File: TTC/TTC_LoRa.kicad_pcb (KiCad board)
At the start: 2 copper layers, 70 x 70 mm, 78 parts, among them J1 EPS 3V3, J2 MISSION, J3 SMA edge, J4 SWD TC2030, J5 OBC I2C, J6 OBC UART, J7 EPS 5V, J8 SPARE GPIO, J9 DIPOLE FEED, Q1 AO3401A, U1 TPS7A2033PDBVR, U2 RFM98W-433S2, U3 STM32F446RET6, U4 TMP102, Y1 8MHz, Y2 32.768kHz

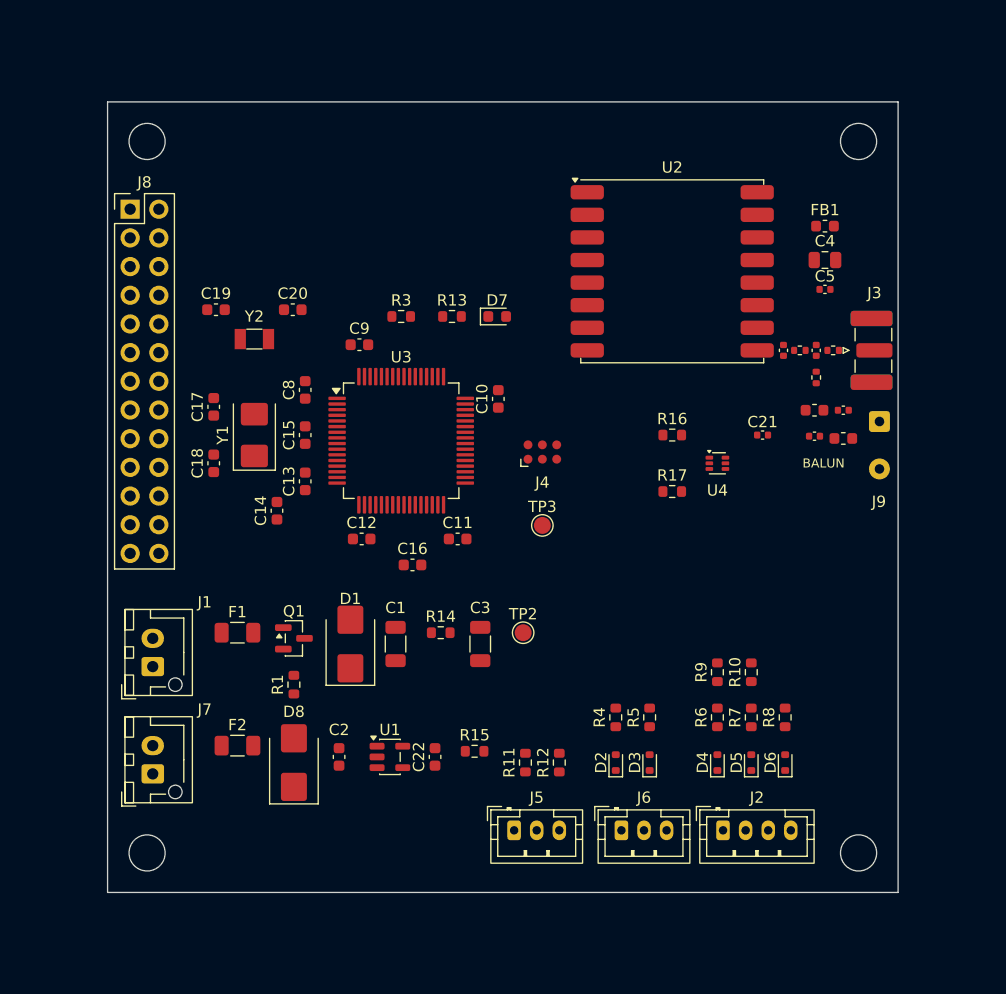
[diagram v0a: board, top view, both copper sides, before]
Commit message: Update ADCS and TTC KiCad designs
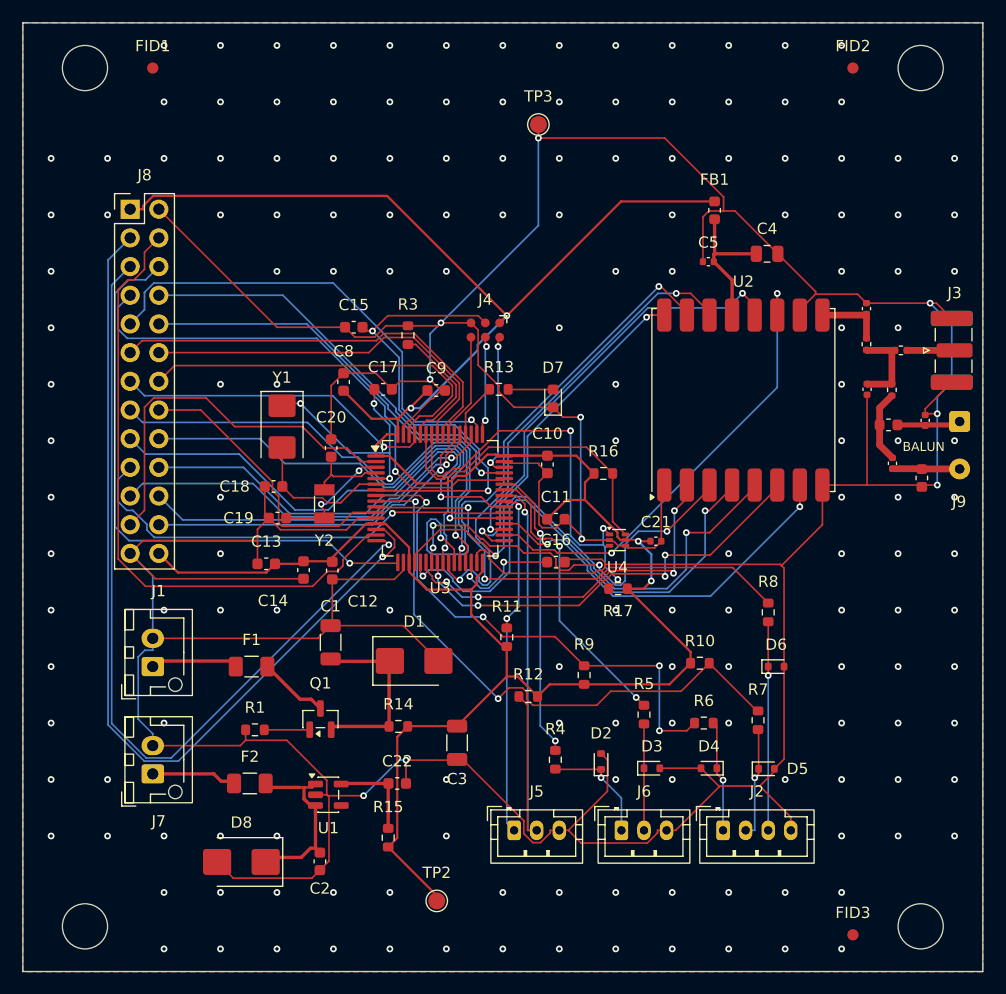
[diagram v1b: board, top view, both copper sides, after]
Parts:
- added FID1: Fiducial, Fiducial_1mm_Mask2mm, F.Cu at (104.0, 97.0)
- added FID2: Fiducial, Fiducial_1mm_Mask2mm, F.Cu at (166.0, 97.0)
- added FID3: Fiducial, Fiducial_1mm_Mask2mm, F.Cu at (166.0, 173.8)
- H1, H2, H3, H4: value M3 -> M4 stack; footprint MountingHole_3.2mm_M3 -> MountingHole_4mm
- moved TP3 35.5 mm to (138.2, 102.0), turned to -90 degrees
- moved TP2 25.0 mm to (129.2, 170.8), turned to 180 degrees
- moved C19 19.2 mm to (115.0, 136.8)
- moved Y2 15.9 mm to (119.2, 135.6), turned to -90 degrees
- moved C17 15.1 mm to (124.4, 125.5), turned to 180 degrees
- moved C21 13.3 mm to (148.6, 138.9)
- moved U2 13.0 mm to (156.3, 126.4), turned to 90 degrees
- moved C20 12.7 mm to (119.8, 130.7), turned to -90 degrees
- moved C16 12.7 mm to (139.7, 140.8)
- moved J4 11.9 mm to (133.4, 120.2), turned to 180 degrees
- moved R9 11.8 mm to (142.2, 150.8)
- moved R11 11.2 mm to (135.3, 147.4)
- moved U4 11.2 mm to (145.2, 138.8)
- moved R15 10.8 mm to (124.8, 165.2), turned to -90 degrees
- moved C5 10.6 mm to (153.2, 114.2), turned to 180 degrees
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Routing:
- net GND: track 0.00 -> 499.8 mm, vias 0 -> 172
- net +3V3: track 0.00 -> 234.7 mm, vias 0 -> 4
- net /PA0: track 0.00 -> 81.2 mm, vias 0 -> 1
- net /PA2: track 0.00 -> 76.0 mm, vias 0 -> 1
- net /PA1: track 0.00 -> 56.3 mm
- net /PA3: track 0.00 -> 51.9 mm, vias 0 -> 1
- net /RBF_IN: track 0.00 -> 51.8 mm, vias 0 -> 2
- net /RFM_DIO1: track 0.00 -> 47.4 mm, vias 0 -> 2
- net /PA11: track 0.00 -> 46.6 mm, vias 0 -> 1
- net /SPI1_SCK: track 0.00 -> 46.5 mm, vias 0 -> 2
- net /RFM_NSS: track 0.00 -> 46.3 mm, vias 0 -> 2
- net /DEPLOY_SW: track 0.00 -> 45.6 mm, vias 0 -> 4
- net /PB10: track 0.00 -> 45.2 mm, vias 0 -> 1
- net /OBC_SCL: track 0.00 -> 44.9 mm, vias 0 -> 1
- net /PC5: track 0.00 -> 44.7 mm, vias 0 -> 1
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- added copper zone on B.Cu, net GND
- added copper zone on F.Cu, net GND
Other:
- board size 70 x 70 mm -> 85 x 84 mm
